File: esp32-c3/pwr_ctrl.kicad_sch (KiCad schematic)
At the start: 9 parts, among them U7 TC118S

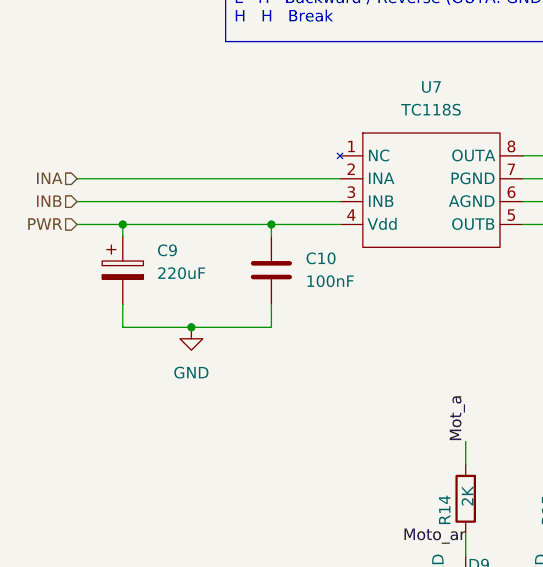
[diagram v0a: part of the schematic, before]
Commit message: Fix Battery power and USB/UART connection, move vent around to accomodate enclosure
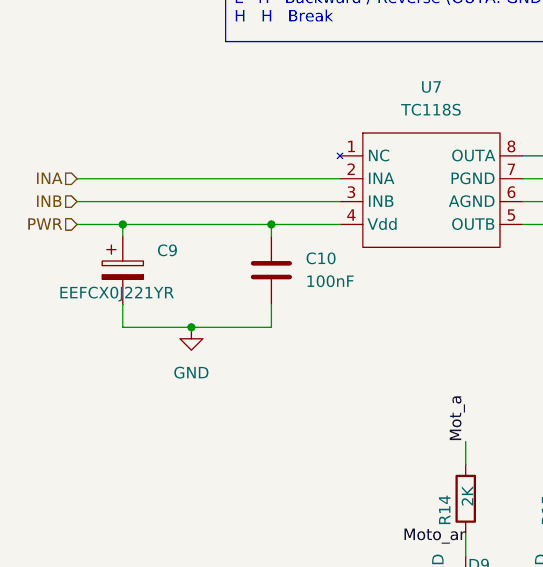
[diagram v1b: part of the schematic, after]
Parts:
- C10, C11, C12: footprint Capacitor_SMD:C_0805_2012Metric -> Capacitor_SMD:C_0402_1005Metric
- C9: value 220uF -> EEFCX0J221YR; footprint Capacitor_Tantalum_SMD:CP_EIA-7343-43_Kemet-X -> local:CP_SMD_4.3x7.3mm; LCSC C7231 -> C1414444
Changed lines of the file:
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@@
 			)
 		)
-		(property "Footprint" "Capacitor_SMD:C_0805_2012Metric"
+		(property "Footprint" "Capacitor_SMD:C_0402_1005Metric"
 			(at 133.0452 78.74 0)
 			(effects
@@
 			)
 		)
-		(property "Footprint" "Capacitor_SMD:C_0805_2012Metric"
+		(property "Footprint" "Capacitor_SMD:C_0402_1005Metric"
 			(at 73.3552 87.63 0)
 			(effects
@@
 		(on_board yes)
 		(dnp no)
-		(fields_autoplaced yes)
 		(property "Reference" "C9"
 			(at 59.69 81.6609 0)
@@
 			)
 		)
-		(property "Value" "220uF"
-			(at 59.69 84.2009 0)
+		(property "Value" "EEFCX0J221YR"
+			(at 48.768 86.36 0)
 			(effects
 				(font
@@
 			)
 		)
-		(property "Footprint" "Capacitor_Tantalum_SMD:CP_EIA-7343-43_Kemet-X"
+		(property "Footprint" "local:CP_SMD_4.3x7.3mm"
 			(at 56.8452 87.63 0)
 			(effects
@@
 			)
 		)
-		(property "LCSC" "C7231"
+		(property "LCSC" "C1414444"
 			(at 55.88 83.82 0)
 			(effects
@@
 			)
 		)
-		(property "Footprint" "Capacitor_SMD:C_0805_2012Metric"
+		(property "Footprint" "Capacitor_SMD:C_0402_1005Metric"
 			(at 120.3452 78.74 0)
 			(effects
